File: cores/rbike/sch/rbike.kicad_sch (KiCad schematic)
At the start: 2 parts

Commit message: wip io
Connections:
- net 1P_BTN_4: now reaches JM1.25 (1P_BTN_4)
- net 2P_BTN_4: now reaches JM1.c (2P_BTN_4)
- net N.C4 renamed TILT
- no-connect marks 4 -> 2
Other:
- removed sheet amplifiers
- removed sheet colmix
- added sheet colmix_rgb (colmix_rgb.kicad_sch)
- sheet io_cabinet ports: added 1P_RIGHT, KEY-2P; removed none
- sheet main ports: added BSPR~{CE}, D1, MAINAND1, MAIN_AB[15..0], MAIN_DB[15..0], MR~{W}, M~{LDS}, M~{Y2}, RAM~{CS1}H, RAM~{OE}, SCU~{CS}, SCU~{RES}, SRST, S~{CLK}, VINT, ~{BUSACK}Q, ~{BUSRQ}, ~{DEC1}, ~{DTACK}; removed none
- sheet objects ports: added BSPR~{CE}, FK[8..0], FOUT[15..0], FO[15..0]; removed none
- sheet scroll ports: added BO[15..0], DCLK1, MAIN_AB[4..0], MAIN_DB[15..0], MR~{W}, ~{ACK}, ~{LDS}; removed none
- note added: "TEST"

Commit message: wip obj
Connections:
- net N.C0 renamed COIN_LOCKOUT1
- net N.C3 renamed COIN_LOCKOUT2
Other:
- sheet colmix_rgb ports: added ~{RESET}; removed SCU~{RES}
- sheet io_cabinet ports: added +12V, 1P_BTN_1, 1P_BTN_2, 1P_BTN_3, 1P_BTN_4, 1P_DOWN, 1P_LEFT, 1P_START, 1P_UP, 2P_BTN_1, 2P_BTN_2, 2P_BTN_3, 2P_BTN_4, 2P_DOWN, 2P_LEFT, 2P_RIGHT, 2P_START, 2P_UP, COIN_1, COIN_2, COIN_CNT_1, COIN_CNT_2, COIN_LOCKOUT1, COIN_LOCKOUT2, DIPSW-1, DIPSW-2, KEY-1P, KEY-TILT, SERVICE, S~{BNK3}, TILT, ~{RESET}; removed none
- sheet main ports: added ~{RESET}; removed SCU~{RES}
- moved on the sheet: ZD?

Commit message: wip spr scr drivers
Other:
- sheet main ports: added MUDS/LDS; removed D1
- sheet sound ports: added SRD, ~{BUSACK}Q, ~{DTACK}; removed PIN 7BCU

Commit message: rbike finished
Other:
- sheet sound ports: added SCLK; removed S~{CLK}

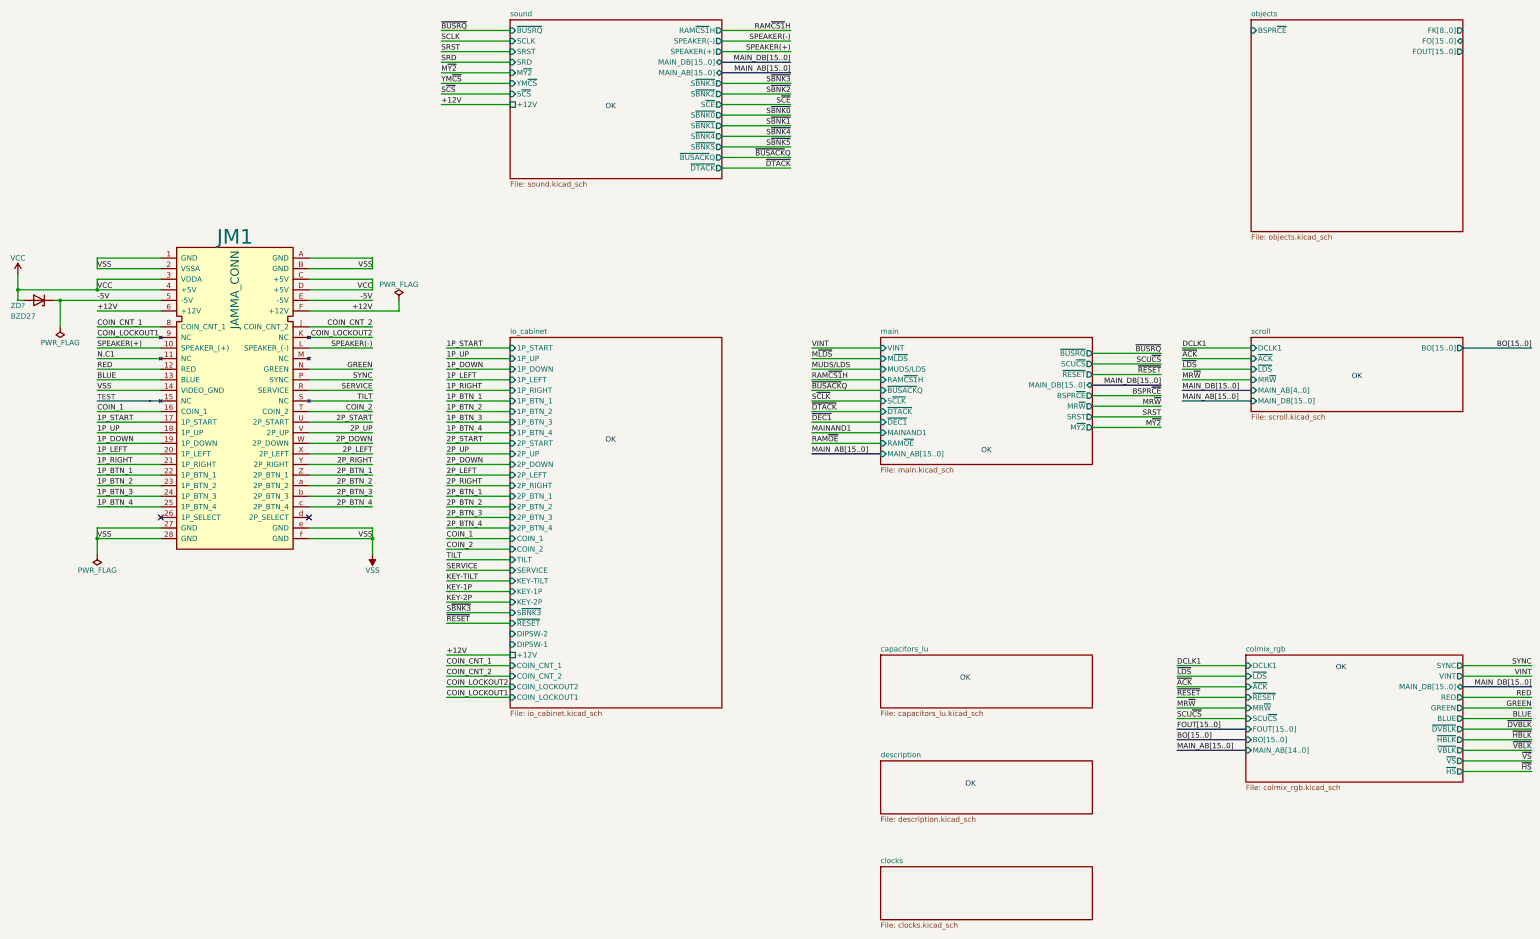
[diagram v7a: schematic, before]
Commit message: rbike control of electrical rules
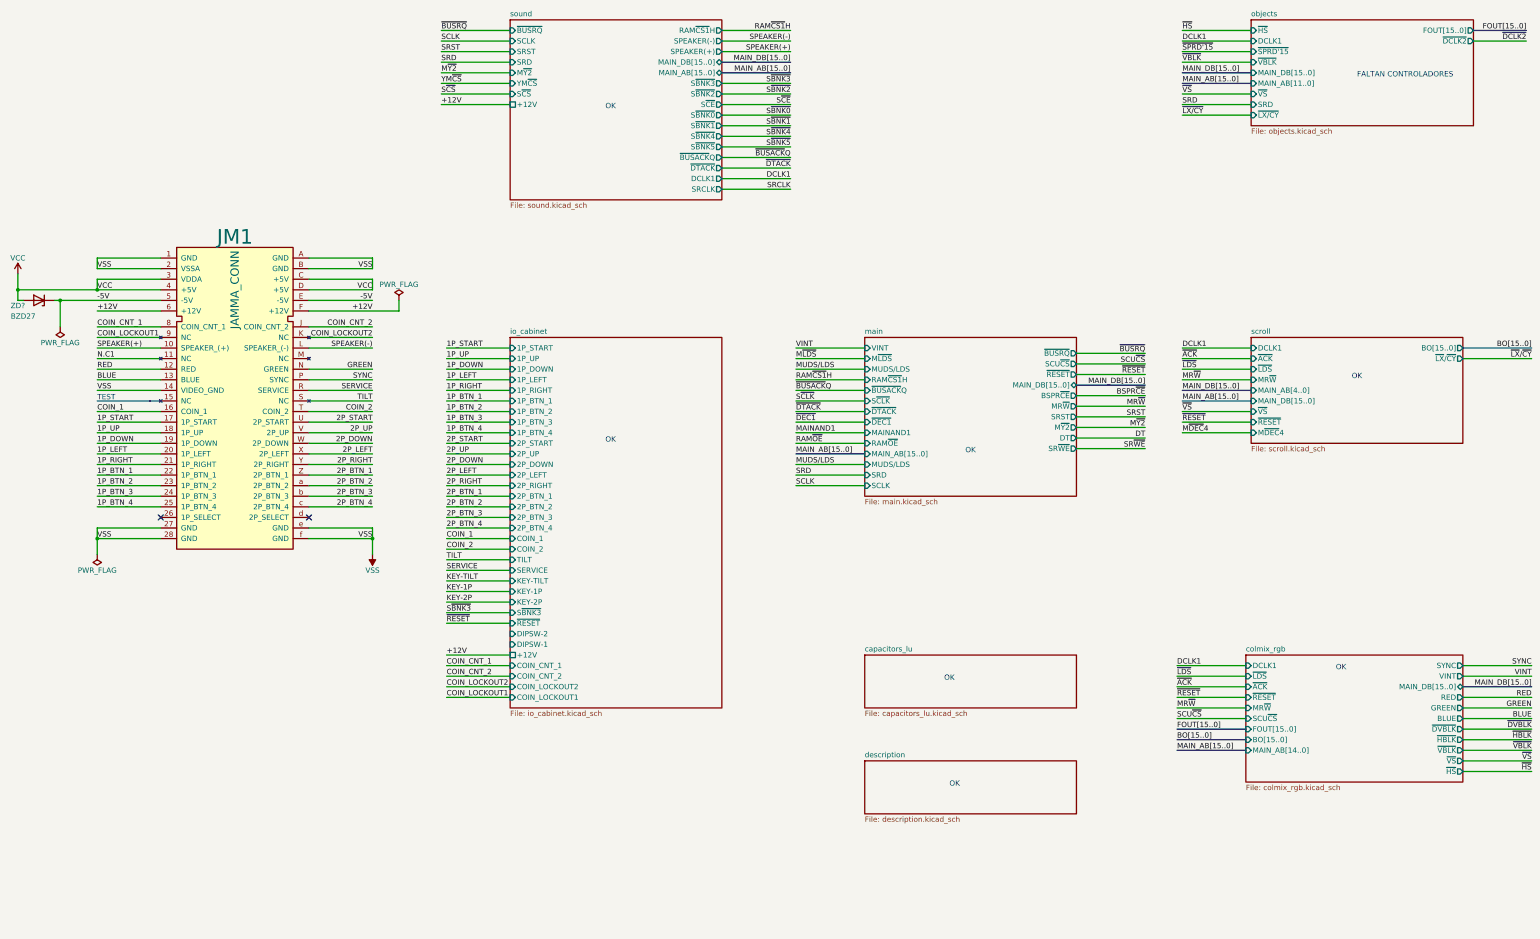
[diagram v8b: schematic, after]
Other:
- removed sheet clocks
- sheet main ports: added DT, MUDS/LDS, SCLK, SRD, SR~{WE}; removed none
- sheet objects ports: added DCLK1, MAIN_AB[11..0], MAIN_DB[15..0], SRD, ~{DCLK2}, ~{HS}, ~{LX/CY}, ~{SPRD'15}, ~{VBLK}, ~{VS}; removed BSPR~{CE}, FK[8..0], FO[15..0]
- sheet scroll ports: added M~{DEC}4, ~{LX}/~{CY}, ~{RESET}, ~{VS}; removed none
- sheet sound ports: added DCLK1, SRCLK; removed none
- note added: "FALTAN CONTROLADORES"
